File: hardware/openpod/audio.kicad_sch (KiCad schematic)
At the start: 29 parts, among them J1 SJ-43515TS-SMT-TR

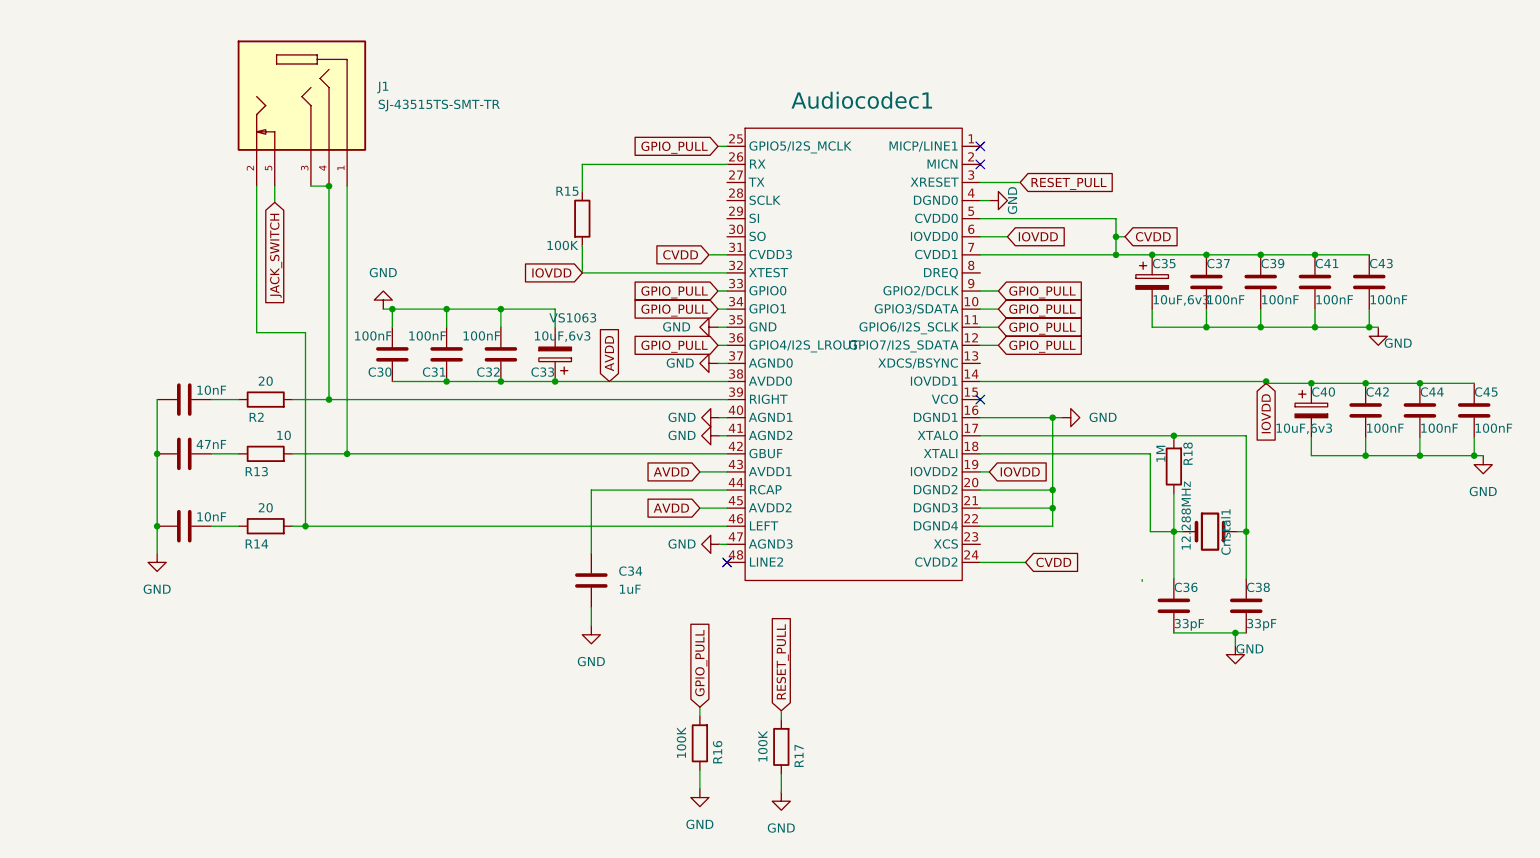
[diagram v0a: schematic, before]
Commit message: Rebirth (#2)
* designed clickwheel and see if mpr121 can fit on it

* update power and audio

* added UART converter

* added bluetooth

* try up with vs1053 feather

* setupt the player file

* fill screen with different colors

* almost works with GFX, just wrong coordinates

* test MADCTL 1

* wrong, screen is all white

* screen pins before remap

* new pinout with consecutive 16bits on the PCs pins

* screen works

* added demo

* updated platformio.ini

* added blog

* cleanup

* first menu

* Fast (ugly) menu renderer

* ugly theme + blog post

* transition using HW scrolling

* breakdown ui

* 30 rows buffer

* remove row/col shit

* added content for the blog

* start restoring render of the now playing

* scroll to nowplaying

* working transitiontotracklist (but slight prolbem with last line)

* fixed the wrapping issue at the bottom

* update theme

* rewired vs1053

* screen and mp3 working

* pins

* updated mp3 pinout to have i2c available

* testing the clickwheel with teleplot: looking good !

* Debugging the wheel: it follows my finger on the screen

* first scrolling the tracks with the wheel !

* WIP

* use an app state and allow to use more bits per pixel

* setup unit tests

* std

* remove select track

* use doctest and reporter

* make tests pass

* cleanup

* fixed scripts

* faster render fonts

* dark background

* better state + events handler system

* wip

* faster renderer of tracklist + animations + better split between concerns

* 2 bits per pixel

* docs

* remove unit tests

* simplify ui list

* rename track to element

* rename track to element

* psram controller

* psram works on SPI1

* psram controller works

* indexer

* crawler

* radix tree?

* update trie generator

* started implementing storage

* trie index

* search works on the stm32

* can retrieve now paths

* sound player on the way

* enhanced mp3 working, but not flac

* flac plugin

* config files

* load flac plugin correctly: saccaded sound

* cleaning up

*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
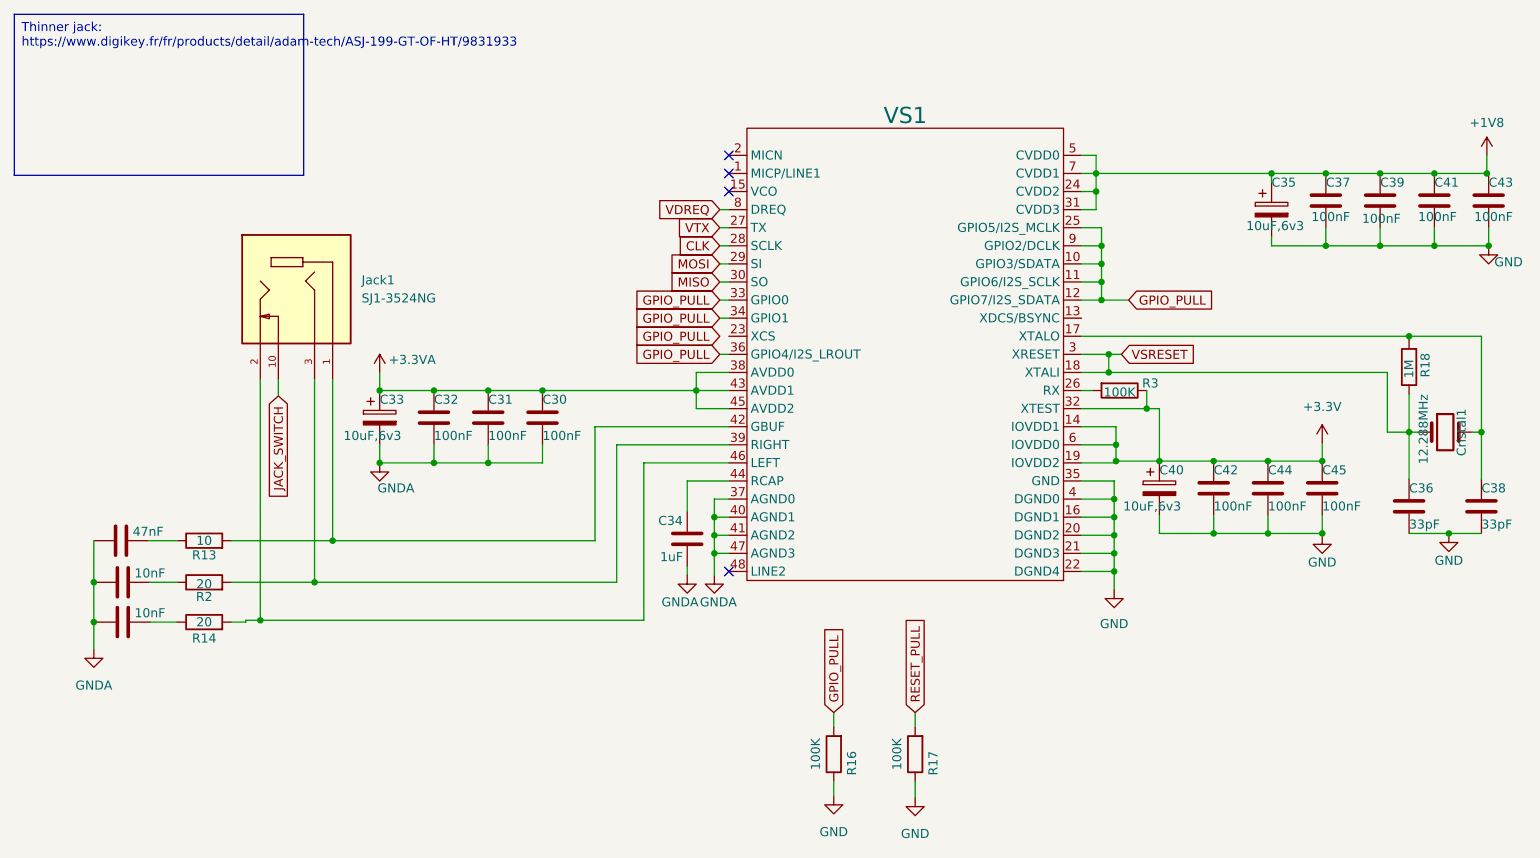
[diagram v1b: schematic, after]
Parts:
- removed Audiocodec1: VS1063, Package_QFP:LQFP-48-1EP_7x7mm_P0.5mm_EP3.6x3.6mm, symbol vs1063:vs1063
- removed J1: SJ-43515TS-SMT-TR, jack:CUI_SJ-43515TS-SMT-TR, symbol jack:SJ-43515TS-SMT-TR
- removed R15: 100K, symbol Device:R
- added Jack1: SJ1-3524NG, openpod:CUI_SJ1-3524NG, symbol openpod:SJ1-3524NG
- added R3: 100K, symbol Device:R
- added VS1: ~, symbol openpod:vs1063
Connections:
- net GND: now also VS1.16 (DGND1), VS1.20 (DGND2), VS1.21 (DGND3), VS1.22 (DGND4), VS1.35 (GND), VS1.4 (DGND0); no longer C29.1, C3.1, C30.2, C31.2, C32.2, C33.2, C34.2, C9.1
- net GPIO_PULL: now also VS1.10 (GPIO3/SDATA), VS1.11 (GPIO6/I2S_SCLK), VS1.12 (GPIO7/I2S_SDATA), VS1.25 (GPIO5/I2S_MCLK), VS1.33 (GPIO0), VS1.34 (GPIO1), VS1.36 (GPIO4/I2S_LROUT), VS1.9 (GPIO2/DCLK)
- net JACK_SWITCH: now also Jack1.10
- net at C34.1: now also VS1.44 (RCAP)
- net at R13.2: now also Jack1.1, VS1.42 (GBUF)
- net at R14.2: now also Jack1.2, VS1.46 (LEFT)
- net at R2.2: now also Jack1.3, VS1.39 (RIGHT)
- net VSRESET: now reaches C36.1, Cristal1.1, R18.1
- net VSRESET: now also VS1.18 (XTALI), VS1.3 (XRESET)
- net at C38.1, Cristal1.2, R18.2: now also VS1.17 (XTALO)
- net AVDD renamed +3.3VA
- net +3.3VA: now also VS1.38 (AVDD0), VS1.43 (AVDD1), VS1.45 (AVDD2)
- net CVDD renamed +1V8
- net +1V8: now also VS1.24 (CVDD2), VS1.31 (CVDD3), VS1.5 (CVDD0), VS1.7 (CVDD1)
- net IOVDD renamed +3.3V
- net +3.3V: now also R3.1, VS1.14 (IOVDD1), VS1.19 (IOVDD2), VS1.32 (XTEST), VS1.6 (IOVDD0)
- new net: R3.2, VS1.26 (RX)
- new net CLK: VS1.28 (SCLK)
- new net GNDA: C29.1, C3.1, C30.2, C31.2, C32.2, C33.2, C34.2, C9.1, VS1.37 (AGND0), VS1.40 (AGND1), VS1.41 (AGND2), VS1.47 (AGND3)
- new net MISO: VS1.30 (SO)
- new net MOSI: VS1.29 (SI)
- new net VDREQ: VS1.8 (DREQ)
- new net VTX: VS1.27 (TX)
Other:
- moved on the sheet: C30, C31, C32, C33, C34, C35, C36, C37, C38, C39, C40, C41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
